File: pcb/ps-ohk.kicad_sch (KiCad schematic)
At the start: 27 parts

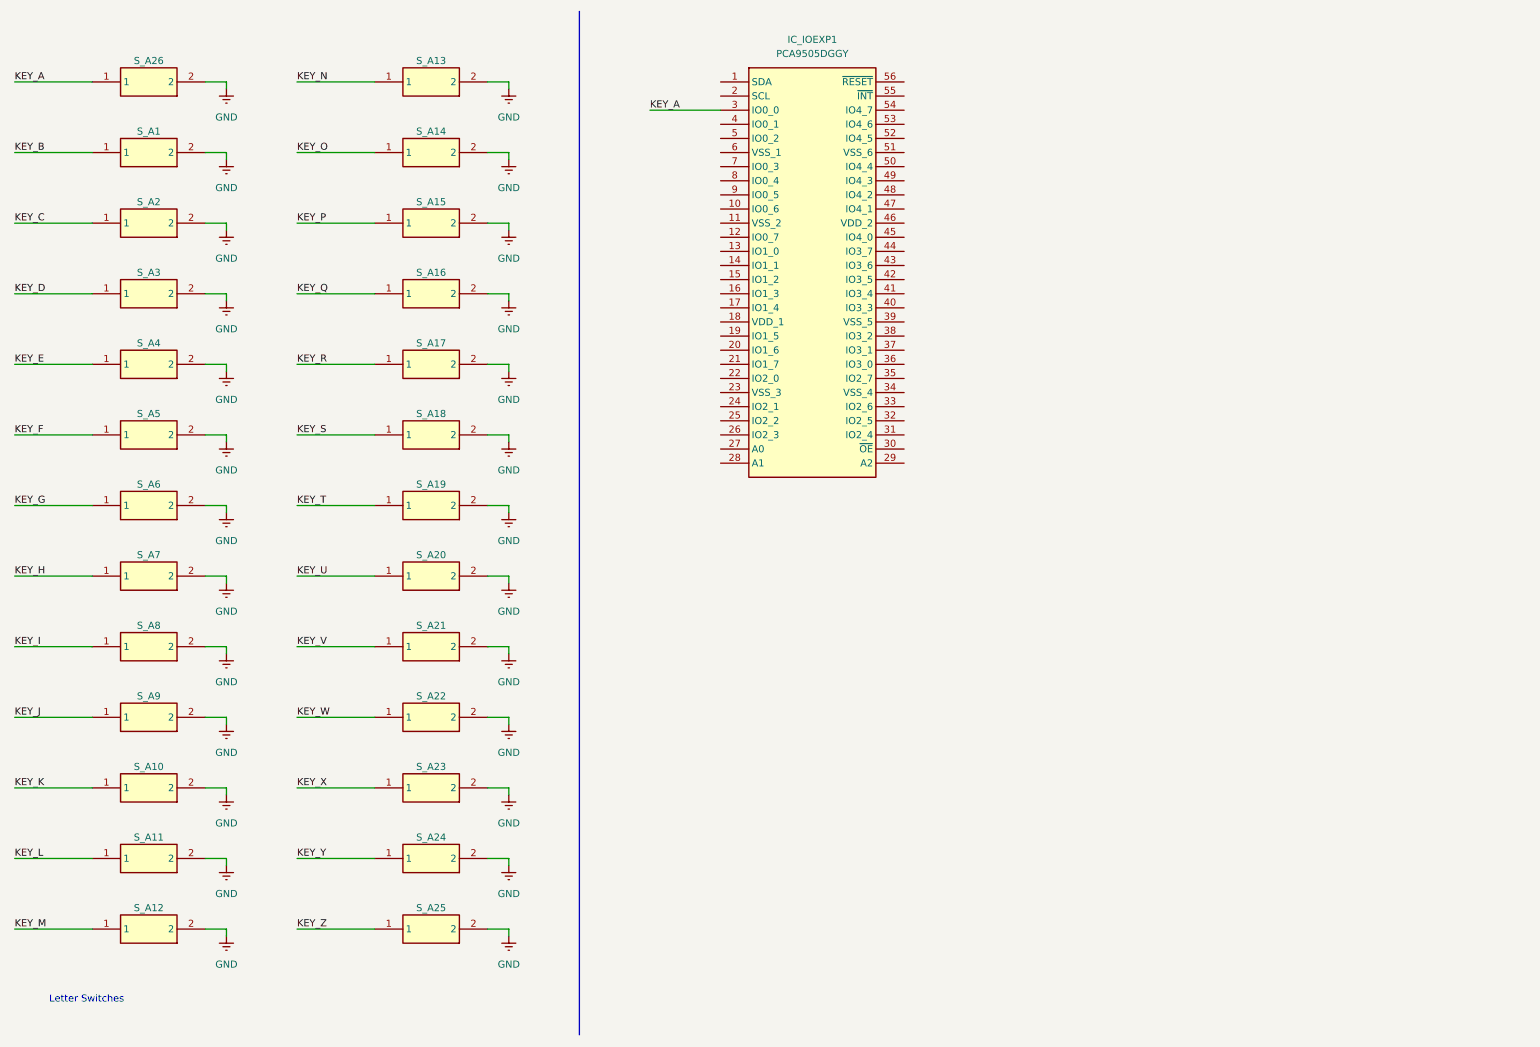
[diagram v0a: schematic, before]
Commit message: pcb: implement IO Expander circuit based on proto
Signed-off-by: Dylan Turner <dylan.turner@tutanota.com>
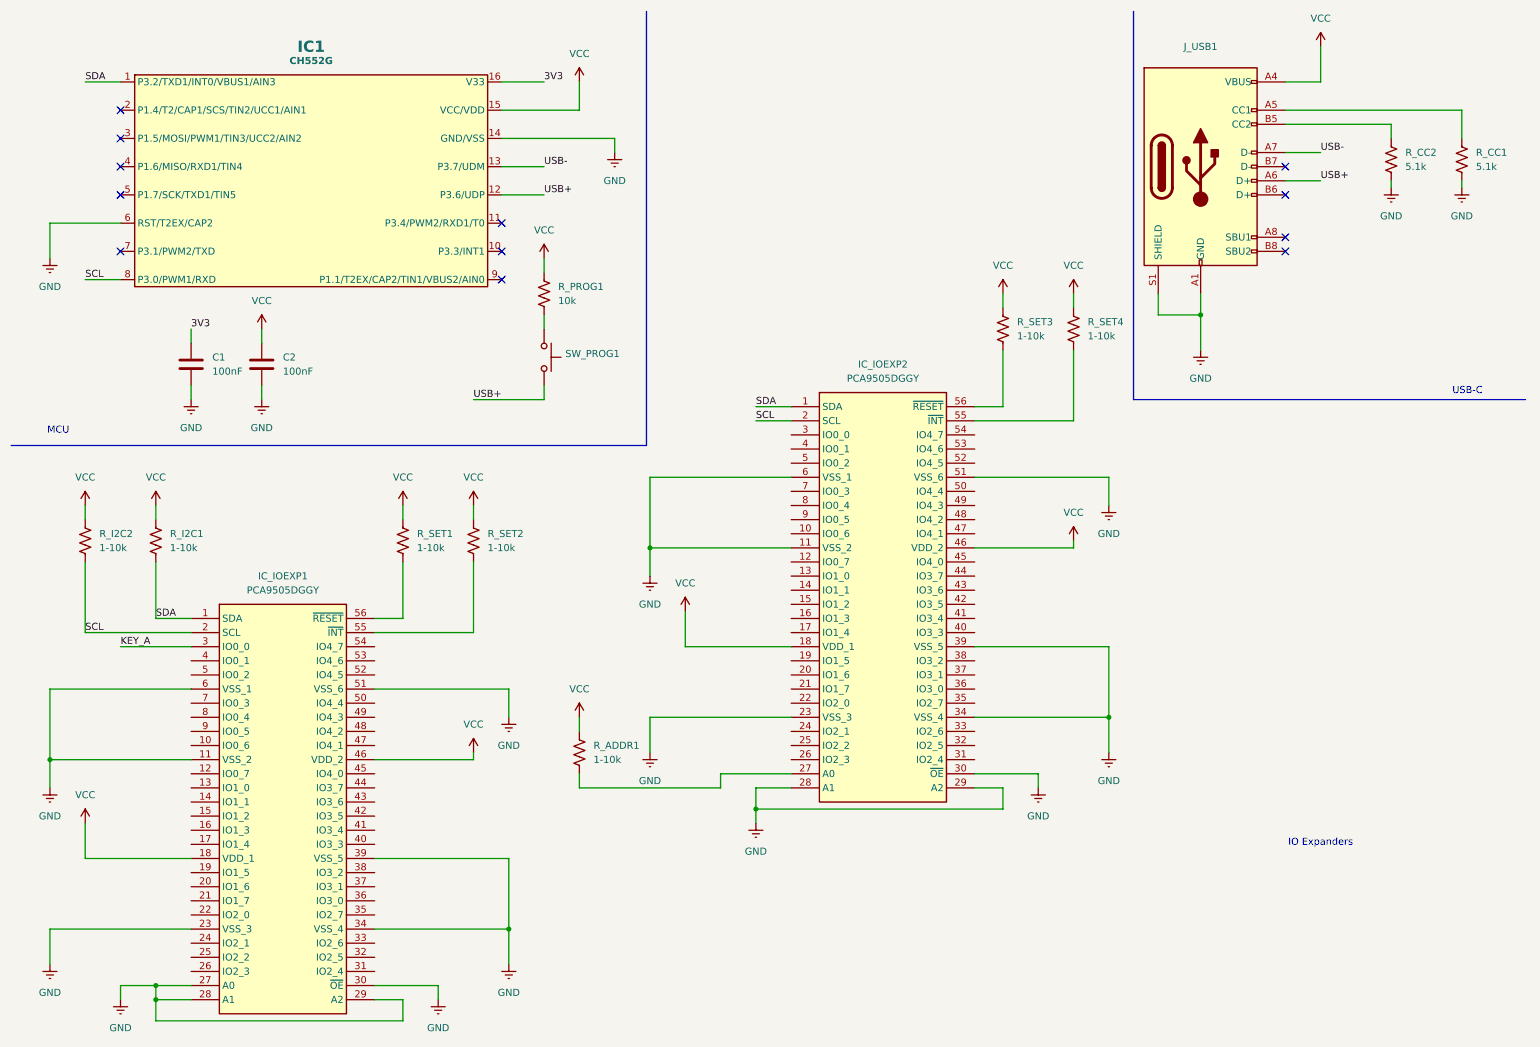
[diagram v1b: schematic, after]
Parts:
- removed S_A1, S_A10, S_A11, S_A12, S_A13, S_A14, S_A15, S_A16, S_A17, S_A18, S_A19, S_A2, S_A20, S_A21, S_A22, S_A23, S_A24, S_A25, S_A26, S_A3, S_A4, S_A5, S_A6, S_A7, S_A8, S_A9: ~, COM-13834:COM13834, symbol COM-13834:COM-13834
- added C1, C2: 100nF, Capacitor_SMD:C_0603_1608Metric, symbol Device:C
- added IC1: CH552G, ch552g:SOIC-16_3.9x9.9mm_Pitch1.27mm, symbol ch552g:CH552G
- added IC_IOEXP2: PCA9505DGGY, PCA9505DGGY:SOP50P810X120-56N, symbol PCA9505DGGY:PCA9505DGGY
- added J_USB1: ~, Connector_USB:USB_C_Receptacle_HCTL_HC-TYPE-C-16P-01A, symbol Connector:USB_C_Receptacle_USB2.0_16P
- added R_ADDR1, R_I2C1, R_I2C2, R_SET1, R_SET2, R_SET3, R_SET4: 1-10k, Resistor_SMD:R_0603_1608Metric, symbol Device:R_US
- added R_CC1, R_CC2: 5.1k, Resistor_SMD:R_0603_1608Metric, symbol Device:R_US
- added R_PROG1: 10k, Resistor_SMD:R_0603_1608Metric, symbol Device:R_US
- added SW_PROG1: ~, Button_Switch_SMD:SW_Push_1P1T_NO_6x6mm_H9.5mm, symbol Switch:SW_Push
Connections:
- net GND: now also IC_IOEXP1.11 (VSS_2), IC_IOEXP1.23 (VSS_3), IC_IOEXP1.27 (A0), IC_IOEXP1.28 (A1), IC_IOEXP1.29 (A2), IC_IOEXP1.30 (~{OE}), IC_IOEXP1.34 (VSS_4), IC_IOEXP1.39 (VSS_5), IC_IOEXP1.51 (VSS_6), IC_IOEXP1.6 (VSS_1), C1.2, C2.2, IC1.14 (GND/VSS), IC1.6 (RST/T2EX/CAP2), IC_IOEXP2.11 (VSS_2), IC_IOEXP2.23 (VSS_3), IC_IOEXP2.28 (A1), IC_IOEXP2.29 (A2), IC_IOEXP2.30 (~{OE}), IC_IOEXP2.34 (VSS_4), IC_IOEXP2.39 (VSS_5), IC_IOEXP2.51 (VSS_6), IC_IOEXP2.6 (VSS_1), J_USB1.A1 (GND), J_USB1.A12 (GND), J_USB1.B1 (GND), J_USB1.B12 (GND), J_USB1.S1 (SHIELD), R_CC1.2, R_CC2.2
- net SDA: now reaches IC_IOEXP1.1 (SDA)
- net SDA: now also IC1.1 (P3.2/TXD1/INT0/VBUS1/AIN3), IC_IOEXP2.1 (SDA), R_I2C1.2
- net VCC: now reaches IC_IOEXP1.18 (VDD_1)
- net VCC: now also IC_IOEXP1.46 (VDD_2), C2.1, IC1.15 (VCC/VDD), IC_IOEXP2.18 (VDD_1), IC_IOEXP2.46 (VDD_2), J_USB1.A4 (VBUS), J_USB1.A9 (VBUS), J_USB1.B4 (VBUS), J_USB1.B9 (VBUS), R_ADDR1.1, R_I2C1.1, R_I2C2.1, R_PROG1.1, R_SET1.1, R_SET2.1, R_SET3.1, R_SET4.1
- net SCL: now reaches IC_IOEXP1.2 (SCL)
- net SCL: now also IC1.8 (P3.0/PWM1/RXD), IC_IOEXP2.2 (SCL), R_I2C2.2
- net at IC_IOEXP1.55 (~{INT}): now also R_SET2.2
- net at IC_IOEXP1.56 (~{RESET}): now also R_SET1.2
- new net: R_PROG1.2, SW_PROG1.1
- new net: IC_IOEXP2.56 (~{RESET}), R_SET3.2
- new net: J_USB1.A5 (CC1), R_CC1.1
- new net: J_USB1.B5 (CC2), R_CC2.1
- new net: IC_IOEXP2.27 (A0), R_ADDR1.2
- new net: IC_IOEXP2.55 (~{INT}), R_SET4.2
- new net 3V3: C1.1, IC1.16 (V33)
- new net USB+: IC1.12 (P3.6/UDP), J_USB1.A6 (D+), SW_PROG1.2
- new net USB-: IC1.13 (P3.7/UDM), J_USB1.A7 (D-)
- no-connect marks 0 -> 12
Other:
- note added: "IO Expanders"
- note added: "MCU"
- note added: "USB-C"
- note removed: "Letter Switches"
- title: PS-OHK -> PS-OHK Control
- moved on the sheet: IC_IOEXP1

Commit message: pcb: add buttons and route
Signed-off-by: Dylan Turner <dylan.turner@tutanota.com>
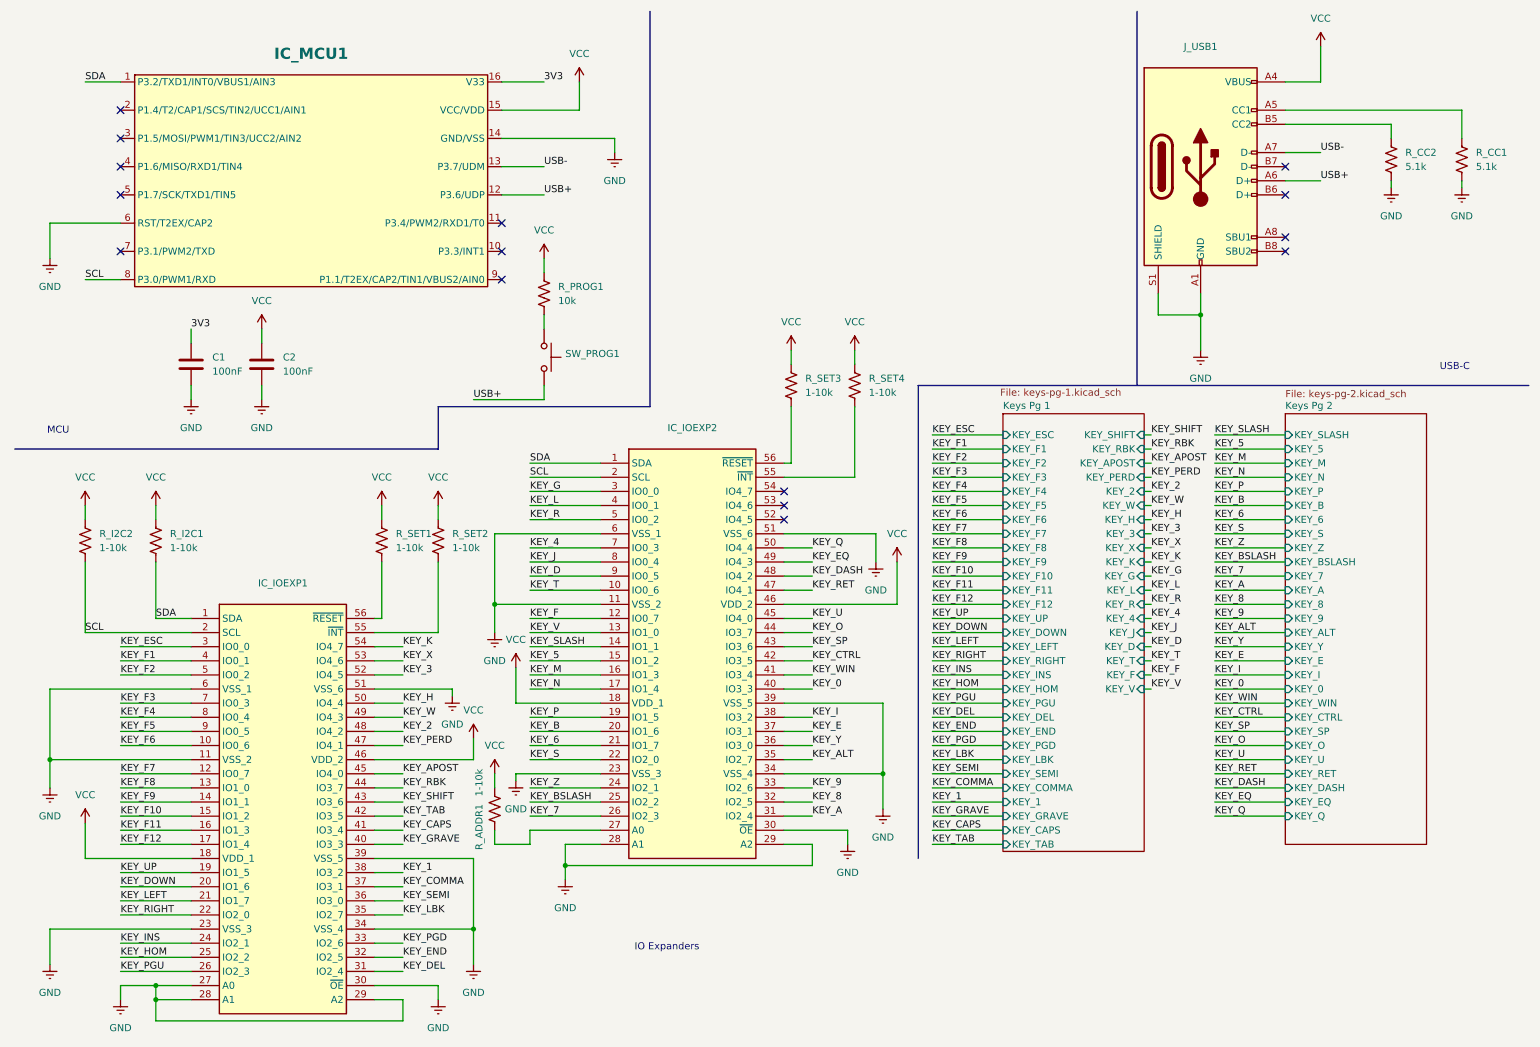
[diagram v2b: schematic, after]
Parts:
- IC_IOEXP1, IC_IOEXP2: value PCA9505DGGY -> ~
- IC_MCU1: renamed from IC1; value CH552G -> ~
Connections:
- net KEY_A: now also IC_IOEXP2.31 (IO2_4); no longer IC_IOEXP1.3 (IO0_0)
- net KEY_F6: now reaches IC_IOEXP1.10 (IO0_6)
- net KEY_F7: now reaches IC_IOEXP1.12 (IO0_7)
- net KEY_F8: now reaches IC_IOEXP1.13 (IO1_0)
- net KEY_F9: now reaches IC_IOEXP1.14 (IO1_1)
- net KEY_F10: now reaches IC_IOEXP1.15 (IO1_2)
- net KEY_F11: now reaches IC_IOEXP1.16 (IO1_3)
- net KEY_F12: now reaches IC_IOEXP1.17 (IO1_4)
- net KEY_UP: now reaches IC_IOEXP1.19 (IO1_5)
- net KEY_DOWN: now reaches IC_IOEXP1.20 (IO1_6)
- net KEY_LEFT: now reaches IC_IOEXP1.21 (IO1_7)
- net KEY_RIGHT: now reaches IC_IOEXP1.22 (IO2_0)
- net KEY_INS: now reaches IC_IOEXP1.24 (IO2_1)
- net KEY_HOM: now reaches IC_IOEXP1.25 (IO2_2)
- net KEY_PGU: now reaches IC_IOEXP1.26 (IO2_3)
- net KEY_DEL: now reaches IC_IOEXP1.31 (IO2_4)
- net KEY_END: now reaches IC_IOEXP1.32 (IO2_5)
- net KEY_PGD: now reaches IC_IOEXP1.33 (IO2_6)
- net KEY_LBK: now reaches IC_IOEXP1.35 (IO2_7)
- net KEY_SEMI: now reaches IC_IOEXP1.36 (IO3_0)
- net KEY_COMMA: now reaches IC_IOEXP1.37 (IO3_1)
- net KEY_1: now reaches IC_IOEXP1.38 (IO3_2)
- net KEY_F1: now reaches IC_IOEXP1.4 (IO0_1)
- net KEY_GRAVE: now reaches IC_IOEXP1.40 (IO3_3)
- net KEY_CAPS: now reaches IC_IOEXP1.41 (IO3_4)
- net KEY_TAB: now reaches IC_IOEXP1.42 (IO3_5)
- net KEY_SHIFT: now reaches IC_IOEXP1.43 (IO3_6)
- net KEY_RBK: now reaches IC_IOEXP1.44 (IO3_7)
- net KEY_APOST: now reaches IC_IOEXP1.45 (IO4_0)
- net KEY_PERD: now reaches IC_IOEXP1.47 (IO4_1)
- net KEY_2: now reaches IC_IOEXP1.48 (IO4_2)
- net KEY_W: now reaches IC_IOEXP1.49 (IO4_3)
- net KEY_F2: now reaches IC_IOEXP1.5 (IO0_2)
- net KEY_H: now reaches IC_IOEXP1.50 (IO4_4)
- net KEY_3: now reaches IC_IOEXP1.52 (IO4_5)
- net KEY_X: now reaches IC_IOEXP1.53 (IO4_6)
- net KEY_K: now reaches IC_IOEXP1.54 (IO4_7)
- net KEY_F3: now reaches IC_IOEXP1.7 (IO0_3)
- net KEY_F4: now reaches IC_IOEXP1.8 (IO0_4)
- net KEY_F5: now reaches IC_IOEXP1.9 (IO0_5)
- net KEY_T: now reaches IC_IOEXP2.10 (IO0_6)
- net KEY_F: now reaches IC_IOEXP2.12 (IO0_7)
- net KEY_V: now reaches IC_IOEXP2.13 (IO1_0)
- net KEY_SLASH: now reaches IC_IOEXP2.14 (IO1_1)
- net KEY_5: now reaches IC_IOEXP2.15 (IO1_2)
- net KEY_M: now reaches IC_IOEXP2.16 (IO1_3)
- net KEY_N: now reaches IC_IOEXP2.17 (IO1_4)
- net KEY_P: now reaches IC_IOEXP2.19 (IO1_5)
- net KEY_B: now reaches IC_IOEXP2.20 (IO1_6)
- net KEY_6: now reaches IC_IOEXP2.21 (IO1_7)
- net KEY_S: now reaches IC_IOEXP2.22 (IO2_0)
- net KEY_Z: now reaches IC_IOEXP2.24 (IO2_1)
- net KEY_BSLASH: now reaches IC_IOEXP2.25 (IO2_2)
- net KEY_7: now reaches IC_IOEXP2.26 (IO2_3)
- net KEY_G: now reaches IC_IOEXP2.3 (IO0_0)
- net KEY_8: now reaches IC_IOEXP2.32 (IO2_5)
- net KEY_9: now reaches IC_IOEXP2.33 (IO2_6)
- net KEY_ALT: now reaches IC_IOEXP2.35 (IO2_7)
- net KEY_Y: now reaches IC_IOEXP2.36 (IO3_0)
- net KEY_E: now reaches IC_IOEXP2.37 (IO3_1)
- net KEY_I: now reaches IC_IOEXP2.38 (IO3_2)
- net KEY_L: now reaches IC_IOEXP2.4 (IO0_1)
- net KEY_0: now reaches IC_IOEXP2.40 (IO3_3)
- net KEY_WIN: now reaches IC_IOEXP2.41 (IO3_4)
- net KEY_CTRL: now reaches IC_IOEXP2.42 (IO3_5)
- net KEY_SP: now reaches IC_IOEXP2.43 (IO3_6)
- net KEY_O: now reaches IC_IOEXP2.44 (IO3_7)
- net KEY_U: now reaches IC_IOEXP2.45 (IO4_0)
- net KEY_RET: now reaches IC_IOEXP2.47 (IO4_1)
- net KEY_DASH: now reaches IC_IOEXP2.48 (IO4_2)
- net KEY_EQ: now reaches IC_IOEXP2.49 (IO4_3)
- net KEY_R: now reaches IC_IOEXP2.5 (IO0_2)
- net KEY_Q: now reaches IC_IOEXP2.50 (IO4_4)
- net KEY_4: now reaches IC_IOEXP2.7 (IO0_3)
- net KEY_J: now reaches IC_IOEXP2.8 (IO0_4)
- net KEY_D: now reaches IC_IOEXP2.9 (IO0_5)
- new net KEY_ESC: IC_IOEXP1.3 (IO0_0)
- no-connect marks 12 -> 15
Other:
- added sheet Keys Pg 1 (keys-pg-1.kicad_sch)
- added sheet Keys Pg 2 (keys-pg-2.kicad_sch)
- title: PS-OHK Control -> PS-OHK Keyboard Controls
- moved on the sheet: IC_IOEXP2, R_ADDR1, R_SET1, R_SET2, R_SET3, R_SET4

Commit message: pcb: made orderable on pcb-way
Signed-off-by: Dylan Turner <dylan.turner@tutanota.com>
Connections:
- net USB+: now also J_USB1.B6 (D+)
- net USB-: now also J_USB1.B7 (D-)
- no-connect marks 15 -> 13
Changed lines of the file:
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@@
+	)
+	(junction
+		(at 243.84 43.18)
+		(diameter 0)
+		(color 0 0 0 0)
 	)
 	(junction
@@
 	)
 	(junction
+		(at 243.84 38.1)
+		(diameter 0)
+		(color 0 0 0 0)
+	)
+	(junction
 		(at 95.25 177.8)
 		(diameter 0)
@@
 	)
 	(no_connect
-		(at 241.3 45.72)
-	)
-	(no_connect
 		(at 31.75 55.88)
 	)
@@
 	)
 	(no_connect
-		(at 241.3 40.64)
-	)
-	(no_connect
 		(at 31.75 40.64)
 	)
@@
 	(wire
 		(pts
+			(xy 243.84 38.1) (xy 247.65 38.1)
+		)
+		(stroke
+			(width 0)
+			(type default)
+		)
+	)
+	(wire
+		(pts
 			(xy 105.41 96.52) (xy 118.11 96.52)
 		)
@@
 	(wire
 		(pts
+			(xy 243.84 40.64) (xy 243.84 38.1)
+		)
+		(stroke
+			(width 0)
+			(type default)
+		)
+	)
+	(wire
+		(pts
 			(xy 99.06 149.86) (xy 99.06 152.4)
 		)
@@
 	(wire
 		(pts
+			(xy 241.3 40.64) (xy 243.84 40.64)
+		)
+		(stroke
+			(width 0)
+			(type default)
+		)
+	)
+	(wire
+		(pts
 			(xy 31.75 170.18) (xy 44.45 170.18)
 		)
@@
 	(wire
 		(pts
+			(xy 243.84 45.72) (xy 243.84 43.18)
+		)
+		(stroke
+			(width 0)
+			(type default)
+		)
+	)
+	(wire
+		(pts
 			(xy 215.9 99.06) (xy 217.17 99.06)
 		)
@@
 	(wire
 		(pts
+			(xy 243.84 43.18) (xy 247.65 43.18)
+		)
+		(stroke
+			(width 0)
+			(type default)
+		)
+	)
+	(wire
+		(pts
 			(xy 77.47 180.34) (xy 82.55 180.34)
 		)
@@
 	(wire
 		(pts
-			(xy 241.3 43.18) (xy 247.65 43.18)
+			(xy 241.3 43.18) (xy 243.84 43.18)
 		)
 		(stroke
@@
 	(wire
 		(pts
-			(xy 241.3 38.1) (xy 247.65 38.1)
+			(xy 241.3 38.1) (xy 243.84 38.1)
 		)
 		(stroke
@@
 		)
 		(stroke
+			(width 0)
+			(type default)
+		)
+	)
+	(wire
+		(pts
+			(xy 241.3 45.72) (xy 243.84 45.72)
+		)
+		(stroke
